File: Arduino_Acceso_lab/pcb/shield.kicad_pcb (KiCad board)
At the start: 2 copper layers, 66 x 53.3 mm, 13 parts, among them K1 RELAY_C, K2 RELAY_C, P10 Analog, P11 Digital, P12 Digital, P13 Timer RTC, P14 Sensor1, P15 Sensor2, P16 Luz1, P17 Luz2, P9 Power

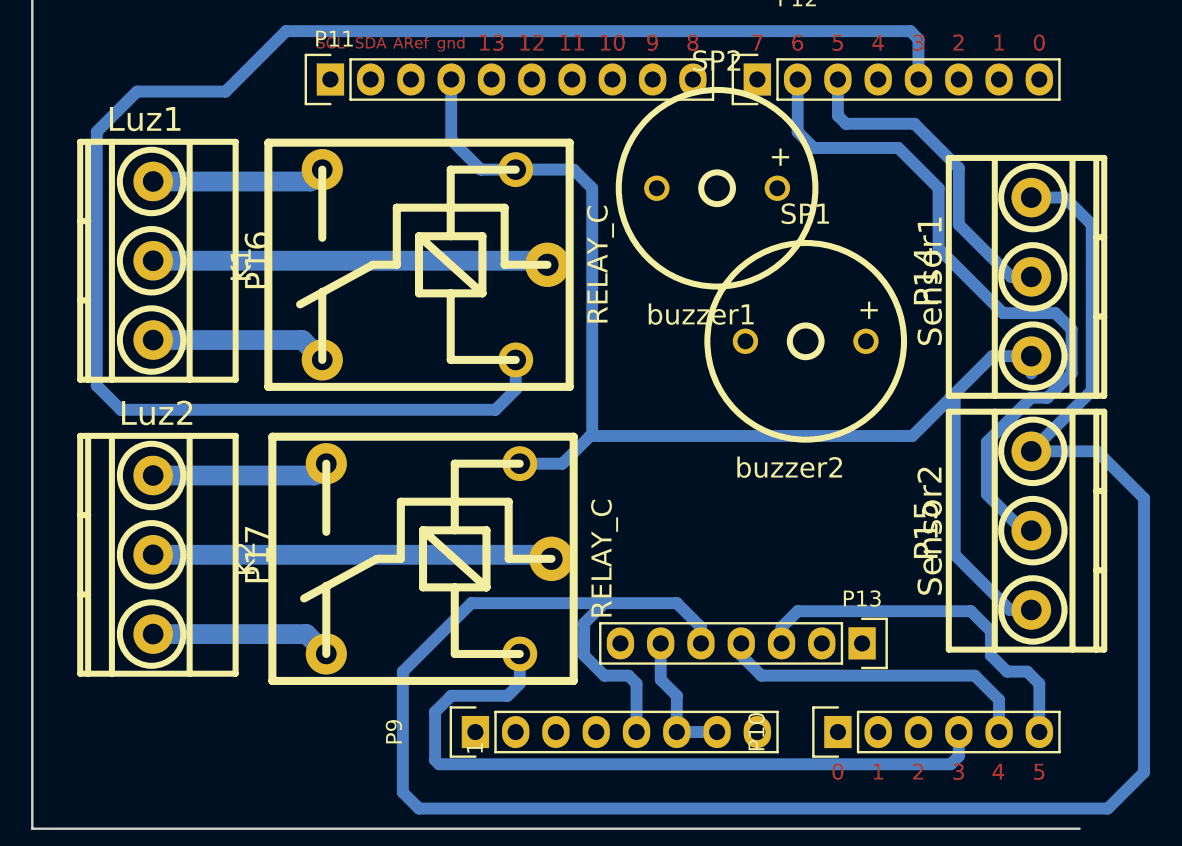
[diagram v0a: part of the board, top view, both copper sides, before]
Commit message: Ordenamiento de bibliotecas y footprints.
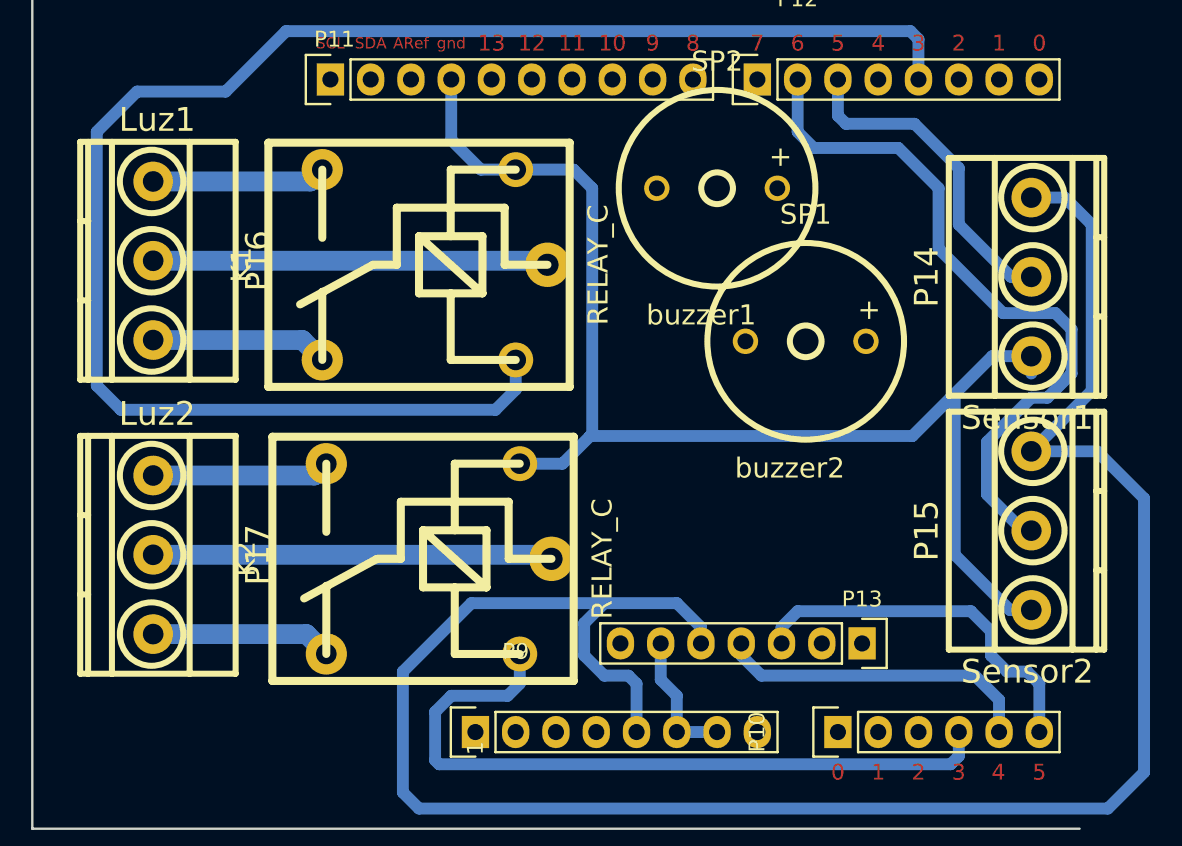
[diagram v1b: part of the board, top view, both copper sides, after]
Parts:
- K1, K2: footprint Poncho_PLC:Relay_C -> huellas:Relay_C
- P10: footprint Pin_Headers:Pin_Header_Straight_1x06 -> huellas:Pin_Header_Straight_1x06
- P11: footprint Pin_Headers:Pin_Header_Straight_1x10 -> huellas:Pin_Header_Straight_1x10
- P12, P9: footprint Pin_Headers:Pin_Header_Straight_1x08 -> huellas:Pin_Header_Straight_1x08
- P13: footprint Socket_Strips:Socket_Strip_Straight_1x07 -> huellas:Socket_Strip_Straight_1x07
- P14, P15: footprint Poncho-PLC:BORNERA3 -> huellas:BORNERA3
- P16, P17: footprint Poncho_PLC:BORNERA3 -> huellas:BORNERA3
- SP1, SP2: footprint Buzzer_Beeper_RevA_25Oct2010:MagneticBuzzer_ProSignal_ABI-009-RC_RevA_25Oct2010 -> huellas:MagneticBuzzer_ProSignal_ABI-009-RC_RevA_25Oct2010
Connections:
- P10 pad 1: /A0 -> (no net)
- P10 pad 2: /A1 -> (no net)
- P10 pad 3: /A2 -> (no net)
- P11 pad 3: /AREF -> (no net)
- P11 pad 5: /13(SCK) -> (no net)
- P11 pad 6: /12(MISO) -> (no net)
- P11 pad 7: /11(**/MOSI) -> (no net)
- P11 pad 8: /10(**/SS) -> (no net)
- P12 pad 1: /7 -> (no net)
- P12 pad 4: /4 -> (no net)
- P12 pad 6: /2 -> (no net)
- P12 pad 7: /1(Tx) -> (no net)
- P12 pad 8: /0(Rx) -> (no net)
- P13 pad 1: Net-(P13-Pad1) -> (no net)
- P13 pad 2: Net-(P13-Pad2) -> (no net)
- P13 pad 7: Net-(P13-Pad7) -> (no net)
- P9 pad 1: Net-(P9-Pad1) -> (no net)
- P9 pad 2: /IOREF -> (no net)
- P9 pad 3: /Reset -> (no net)
- P9 pad 4: /3.3v -> (no net)
- P9 pad 8: /Vin -> (no net)

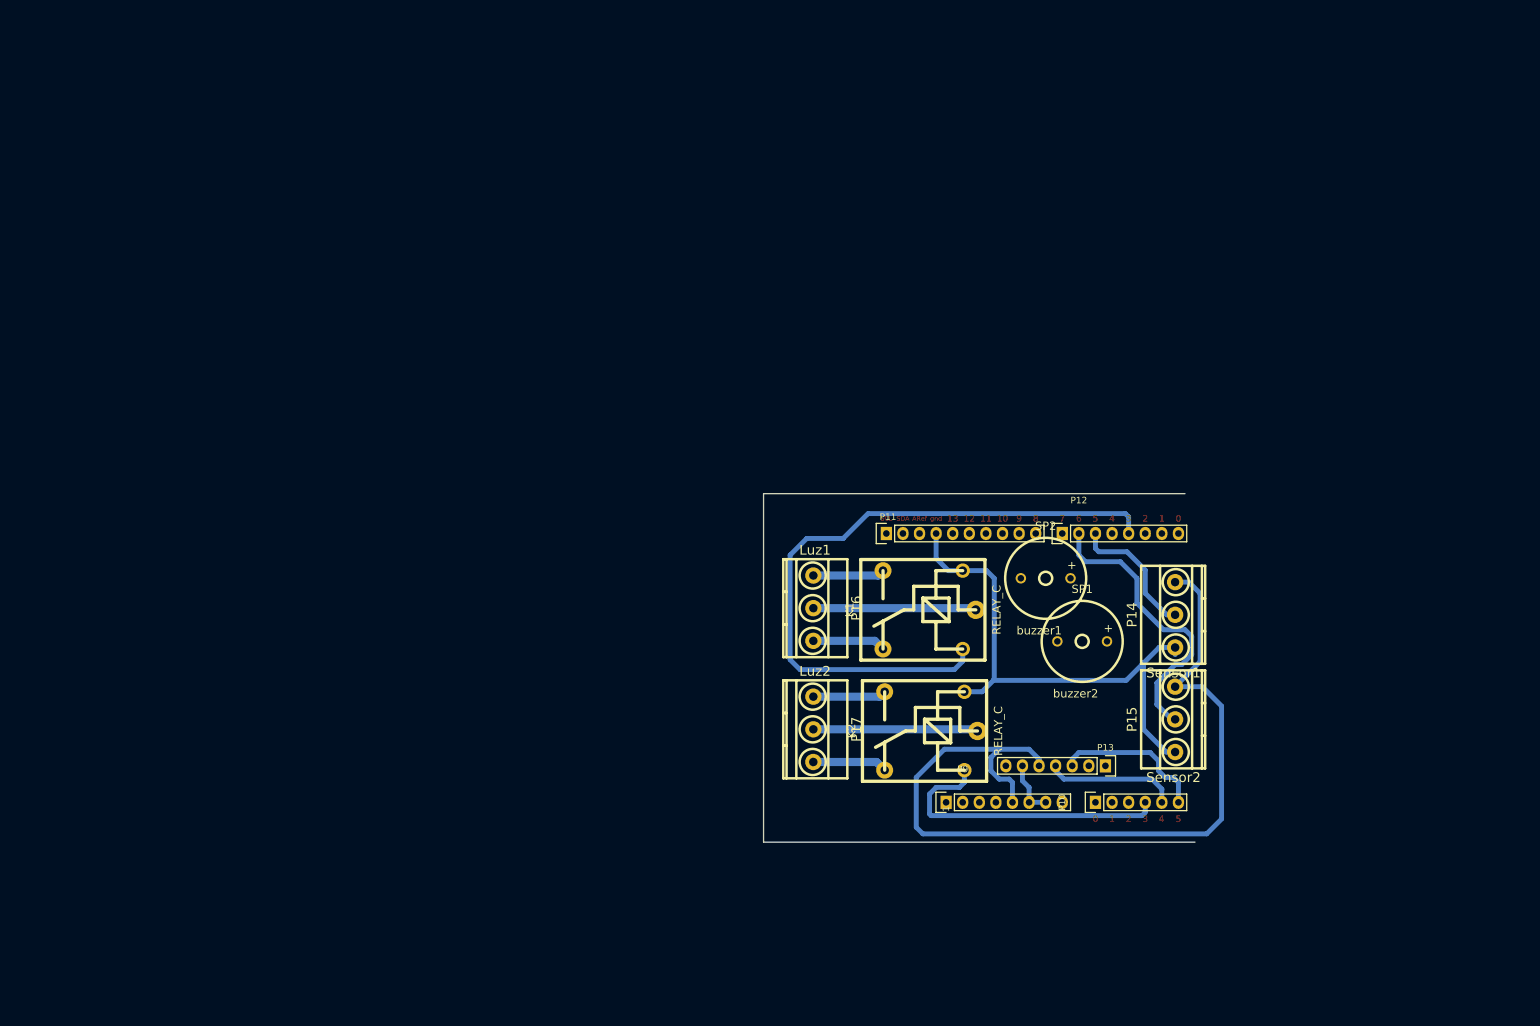
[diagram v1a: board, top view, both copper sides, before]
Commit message: Actualizo pcb del Arduino Acceso lab.
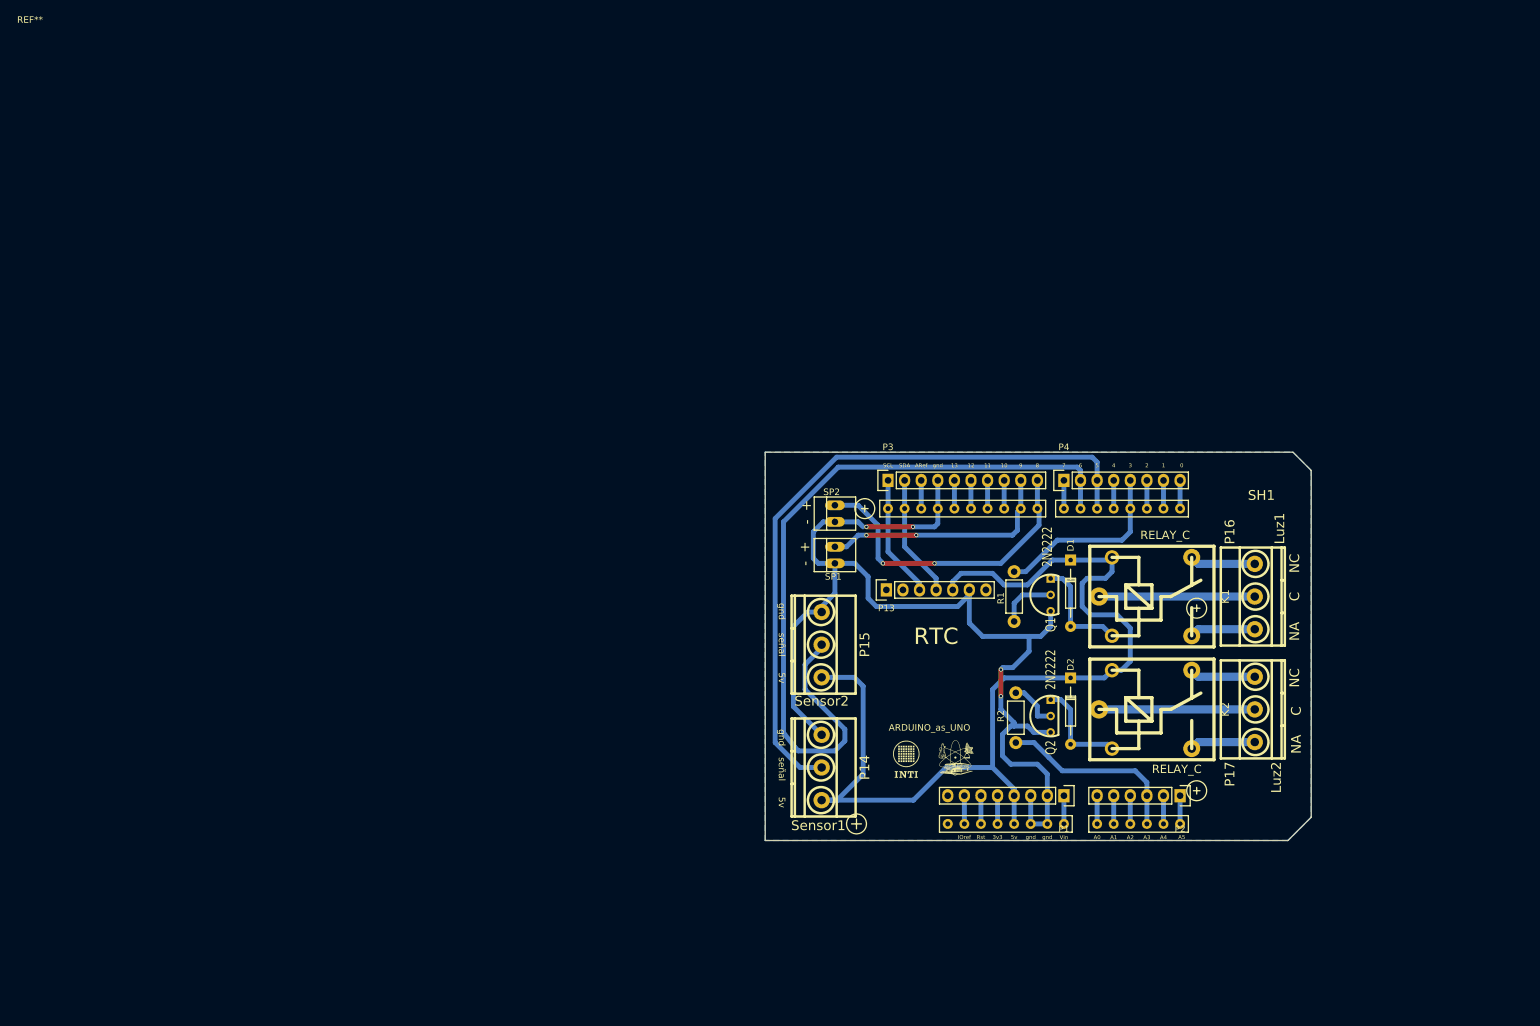
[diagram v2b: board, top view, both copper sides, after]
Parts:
- removed P10: Analog, huellas:Pin_Header_Straight_1x06
- removed P11: Digital, huellas:Pin_Header_Straight_1x10
- removed P12: Digital, huellas:Pin_Header_Straight_1x08
- removed P9: Power, huellas:Pin_Header_Straight_1x08
- added ? (x4): , INTI, F.Cu at (0.00, 0.00)
- added D1: 1N4001, Diodes_ThroughHole:Diode_DO-35_SOD27_Horizontal_RM10, F.Cu at (158.0, 83.2)
- added D2: 1N4001, Diodes_ThroughHole:Diode_DO-35_SOD27_Horizontal_RM10, F.Cu at (158.0, 101.2)
- added G***: LOGO, Poncho_PLC:logoInti, F.Cu at (132.8, 113.7)
- added G***: LOGO, Poncho_PLC:logoInti, B.Cu at (114.0, 70.0)
- added G***: LOGO, Poncho_PLC:logoEscuela, F.Cu at (140.5, 113.4)
- added G***: LOGO, Poncho_PLC:logoInti, F.Cu at (184.4, 74.3)
- added P1: Power, Socket_Strips:Socket_Strip_Straight_1x08, F.Cu at (157.0, 119.3)
- added P2: Analog, Socket_Strips:Socket_Strip_Straight_1x06, F.Cu at (174.8, 119.3)
- added P3: Digital, Socket_Strips:Socket_Strip_Straight_1x10, F.Cu at (130.0, 71.0)
- added P4: Digital, Socket_Strips:Socket_Strip_Straight_1x08, F.Cu at (157.0, 71.0)
- added Q1: 2N2222, kicad:TO92-L21, F.Cu at (154.9, 88.5)
- added Q2: 2N2222, kicad:TO92-L21, F.Cu at (154.9, 107.1)
- added R1: 1K, Resistors_ThroughHole:Resistor_Horizontal_RM7mm, F.Cu at (149.4, 92.6)
- added R2: 1K, Resistors_ThroughHole:Resistor_Horizontal_RM7mm, F.Cu at (149.6, 103.5)
- added REF**: INTI, INTI, F.Cu at (0.00, 0.00)
- added SH1: ARDUINO_as_UNO, SHIELD_ARDUINO:ARDUINO_as_UNO_R3, F.Cu at (145.5, 99.4)
- K1, K2: footprint huellas:Relay_C -> Poncho_PLC:Relay_C
- SP1, SP2: footprint huellas:MagneticBuzzer_ProSignal_ABI-009-RC_RevA_25Oct2010 -> Connect:PINHEAD1-2
- moved P17 67.6 mm to (186.2, 106.0), turned to 90 degrees
- moved P16 67.6 mm to (186.2, 88.8), turned to 90 degrees
- moved P14 58.9 mm to (119.9, 114.9), turned to 270 degrees
- moved P15 55.3 mm to (119.9, 96.1), turned to 270 degrees
- moved P13 43.0 mm to (129.8, 87.8), turned to 0 degrees
- moved SP1 40.1 mm to (121.9, 82.4), turned to 90 degrees
- moved K1 35.1 mm to (170.4, 88.8), turned to 90 degrees
- moved K2 35.0 mm to (170.4, 106.0), turned to 90 degrees
- moved SP2 33.7 mm to (121.9, 76.1), turned to 90 degrees
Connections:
- K1 pad 2: /gnd -> Net-(D1-Pad2)
- K1 pad 5: /3(**) -> /5v
- K2 pad 2: /gnd -> Net-(D2-Pad2)
- K2 pad 5: /A3 -> /5v
- P13 pad 1: (no net) -> Net-(P13-Pad1)
- P13 pad 2: (no net) -> Net-(P13-Pad2)
- P13 pad 3: /A5(SCL) -> Net-(P13-Pad3)
- P13 pad 4: /A4(SDA) -> Net-(P13-Pad4)
- P13 pad 7: (no net) -> Net-(P13-Pad7)
- P14 pad 2: /5(**) -> Net-(P14-Pad2)
- P15 pad 2: /6(**) -> Net-(P15-Pad2)
- SP1 pad 2: /9(**) -> Net-(P3-Pad9)
- SP2 pad 2: /8 -> Net-(P3-Pad10)
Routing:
- net Net-(P15-Pad2): track 0.00 -> 116.9 mm
- net Net-(P14-Pad2): track 0.00 -> 103.6 mm
- net /gnd: track 91.4 -> 165.9 mm, vias 0 -> 4
- net /3(**): track 102.6 -> 28.2 mm
- net Net-(P3-Pad10): track 0.00 -> 47.3 mm, vias 0 -> 2
- net /6(**): track 44.9 -> 0.00 mm
- net Net-(P3-Pad9): track 0.00 -> 37.2 mm, vias 0 -> 2
- net /A5(SCL): track 24.3 -> 0.00 mm
- net /5(**): track 20.8 -> 0.00 mm
- net /A4(SDA): track 20.2 -> 0.00 mm
- net /5v: track 135.4 -> 155.5 mm
- net Net-(P13-Pad4): track 0.00 -> 18.8 mm
- net Net-(P13-Pad3): track 0.00 -> 18.8 mm
- net /A3: track 45.9 -> 28.9 mm
- net Net-(D1-Pad2): track 0.00 -> 16.6 mm
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- added copper zone on B.Cu, net /gnd
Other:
- board size 66 x 53.3 mm -> 83.6 x 59.4 mm
- board text added: "+"
- board text added: "-"
- board text added: "3v3"
- board text added: "5v"
- board text added: "A0"
- board text added: "A1"
- board text added: "A2"
- board text added: "A3"
- board text added: "A4"
- board text added: "A5"
- board text added: "C"
- board text added: "IOref"
- board text added: "NA"
- board text added: "NC"
- board text added: "RTC"
- board text added: "Rst"
- board text added: "Vin"
- board text added: "señal"

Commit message: Arduino Acceso Lab. Ultimas modificaciones al PCB.
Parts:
- removed the G*** at (114.0, 70.0)
- removed the G*** at (184.4, 74.3)
- moved G*** 61.1 mm to (180.6, 75.6)
- moved G*** 59.9 mm to (186.9, 75.6)
- moved P3 8.64 mm to (130.0, 79.6)
- moved P4 8.64 mm to (157.0, 79.6)
- moved SP1 6.61 mm to (121.7, 75.8)
- moved SP2 6.35 mm to (121.9, 82.4)
- moved D1 2.84 mm to (159.3, 85.7)
- moved Q1 2.84 mm to (156.2, 91.1)
- moved P16 2.74 mm to (187.2, 91.3)
- moved R1 2.54 mm to (150.9, 94.6)
- moved K1 2.41 mm to (171.2, 91.1)
- moved P17 2.41 mm to (186.9, 108.3)
- moved D2 2.40 mm to (159.3, 103.3)
- moved K2 2.34 mm to (170.9, 108.3)
- moved Q2 1.80 mm to (156.2, 108.3)
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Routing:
- net /gnd: track 165.9 -> 176.9 mm, vias 4 -> 2
- net Net-(P3-Pad10): track 47.3 -> 40.8 mm
- net Net-(P13-Pad4): track 18.8 -> 14.4 mm
- net Net-(P13-Pad3): track 18.8 -> 14.4 mm
- net Net-(P3-Pad9): track 37.2 -> 41.3 mm
- net /3(**): track 28.2 -> 25.6 mm
- net /5v: track 155.5 -> 157.6 mm
- net /A3: track 28.9 -> 27.3 mm
- net Net-(D1-Pad2): track 16.6 -> 15.7 mm
- net Net-(Q2-Pad2): track 7.70 -> 6.91 mm
- net Net-(Q1-Pad2): track 8.91 -> 8.15 mm
- net Net-(P15-Pad2): track 116.9 -> 117.6 mm
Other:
- board size 83.6 x 59.4 mm -> 83.3 x 59.4 mm

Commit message: Nuevo PCB.
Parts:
- added C1: CP1, Capacitors_ThroughHole:C_Rect_L7.5_W6.5_P5, F.Cu at (196.8, 102.1)
- added C2: CP1, Capacitors_ThroughHole:C_Rect_L7.5_W6.5_P5, F.Cu at (195.6, 122.7)
- added C3: C, Capacitors_ThroughHole:C_Rect_L7.5_W6.5_P5, F.Cu at (205.5, 117.9)
- added D3: D, Resistors_ThroughHole:Resistor_Horizontal_RM7mm, F.Cu at (212.3, 92.7)
- added D4: LED, LEDs:LED-3MM, F.Cu at (196.6, 112.8)
- added L1: INDUCTOR, Inductors:INDUCTOR_V, F.Cu at (203.5, 89.4)
- added P5: modulo esp8266, Socket_Strips:Socket_Strip_Straight_2x04, F.Cu at (195.8, 69.6)
- added P6: fuente, Connect:bornier2, F.Cu at (209.8, 78.0)
- added R3: R, Resistors_ThroughHole:Resistor_Horizontal_RM7mm, F.Cu at (178.9, 78.2)
- added R4: R, Resistors_ThroughHole:Resistor_Horizontal_RM7mm, F.Cu at (178.8, 67.1)
- added R5: R, Resistors_ThroughHole:Resistor_Horizontal_RM7mm, F.Cu at (194.1, 89.4)
- added R6: R, Resistors_ThroughHole:Resistor_Horizontal_RM7mm, F.Cu at (201.9, 95.0)
- added R7: R, Resistors_ThroughHole:Resistor_Horizontal_RM7mm, F.Cu at (210.8, 112.5)
- added U1: LM2576, TO_SOT_Packages_THT:Pentawatt_Neutral_Staggered_Verical_TO220-5-T05D, F.Cu at (210.8, 100.6)
- P7: renamed from SP1; value buzzer2 -> buzzer 1
- P8: renamed from SP2; value buzzer1 -> buzzer 2
- moved ? 219.9 mm to (210.8, 62.5) (x4)
- moved REF** 219.9 mm to (210.8, 62.5)
- moved G*** 77.7 mm to (164.3, 149.9), turned to 90 degrees
- moved G*** 67.0 mm to (114.3, 66.0)
- moved D2 3.57 mm to (159.5, 99.7)
- moved P3 3.57 mm to (130.3, 76.1)
- moved P4 3.57 mm to (157.2, 76.1)
- moved P13 3.57 mm to (187.2, 104.8)
- moved P7 3.57 mm to (121.9, 72.3)
- moved P8 3.57 mm to (122.2, 78.9)
- moved D1 3.57 mm to (159.5, 82.2)
- moved K1 3.57 mm to (171.4, 87.5)
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- renumbered P14 to P10, P15 to P11, P16 to P12, P17 to P13, P13 to P9
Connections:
- net /5v renamed +5P
- net Net-(P1-Pad5) renamed +3.3VP
- net Net-(P4-Pad4) renamed /rx-wifi
- net Net-(P4-Pad6) renamed /tx-wifi
- P1 pad 2: /gnd -> GNDD
- P1 pad 3: /gnd -> GNDD
- P10 pad 1: /gnd -> GNDD
- P11 pad 1: /gnd -> GNDD
- P3 pad 4: /gnd -> Net-(P3-Pad4)
- P7 pad 1: /gnd -> GNDD
- P8 pad 1: /gnd -> GNDD
- P9 pad 6: /gnd -> GNDD
- Q1 pad 1: /gnd -> GNDD
- Q2 pad 1: /gnd -> GNDD
- SH1 pad GND1: /gnd -> GNDD
- SH1 pad GND2: /gnd -> GNDD
- SH1 pad GND3: /gnd -> Net-(P3-Pad4)
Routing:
- net /gnd: track 176.9 -> 0.00 mm, vias 2 -> 0
- net +3.3VP: track 4.32 -> 113.4 mm, vias 0 -> 2
- net Net-(C2-Pad1): track 0.00 -> 54.6 mm, vias 0 -> 4
- net Net-(P11-Pad2): track 117.6 -> 75.9 mm
- net /rx-wifi: track 4.32 -> 44.8 mm, vias 0 -> 2
- net Net-(C1-Pad1): track 0.00 -> 35.5 mm, vias 0 -> 2
- net Net-(P5-Pad7): track 0.00 -> 32.1 mm, vias 0 -> 2
- net Net-(R6-Pad2): track 0.00 -> 27.4 mm, vias 0 -> 2
- net GNDD: track 0.00 -> 24.4 mm, vias 0 -> 1
- net +5P: track 157.6 -> 179.8 mm
- net Net-(D3-Pad1): track 0.00 -> 16.9 mm
- net /tx-wifi: track 4.32 -> 15.0 mm
- net Net-(P3-Pad4): track 0.00 -> 5.84 mm
- net (no net): track 0.00 -> 5.25 mm
- net Net-(P3-Pad2): track 14.4 -> 19.5 mm
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- added copper zone on B.Cu, net GNDD
- removed copper zone on B.Cu, net /gnd
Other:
- board size 83.3 x 59.4 mm -> 103.1 x 65.5 mm
- net class Default: clearance 0.2 -> 0.7; trace_width 0.25 -> 0.7; via_dia 0.6 -> 1.3; via_drill 0.4 -> 0.75
- rule trace_clearance: 0.2 -> 0.7
- rule trace_min: 0.2 -> 0.7
- rule via_min_drill: 0.3 -> 0.75
- rule via_min_size: 0.4 -> 1.3
- board text added: "3.3"
- board text added: "rx"
- board text added: "tx"
